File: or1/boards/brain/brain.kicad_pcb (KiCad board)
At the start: 4 copper layers, 78 x 39 mm, 99 parts, among them J1 XILINX_JTAG, J2 BARREL_JACK, J3 Conn_01x03, J4 Conn_01x05, J5 CONN_SKY130_TEST_HOST, J6 Conn_01x03, U1 STM32F031-QFN28, U2 XC7S15-1FTGB196C, U3 ADP323, U4 S25FL128SAGBHI300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

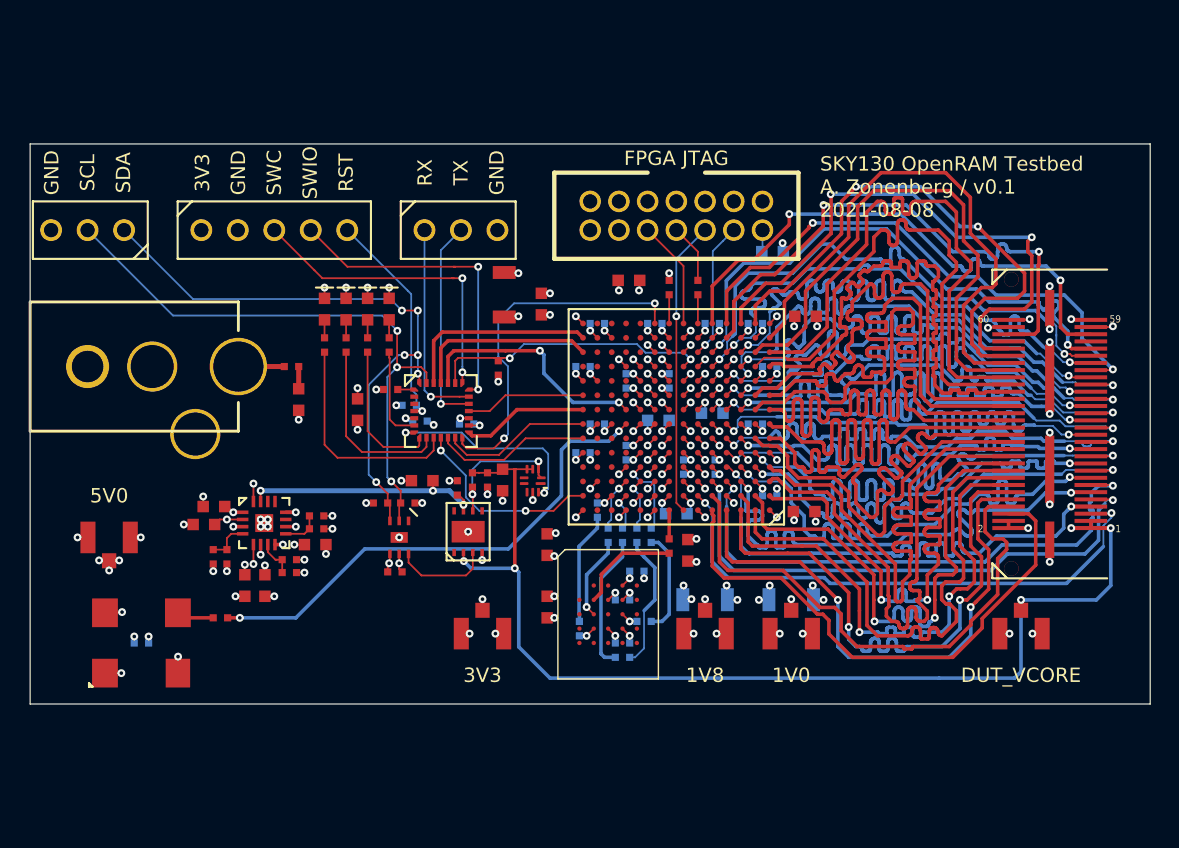
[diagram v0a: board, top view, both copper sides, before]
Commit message: Updated brain board with silkscreen logos and mounting holes
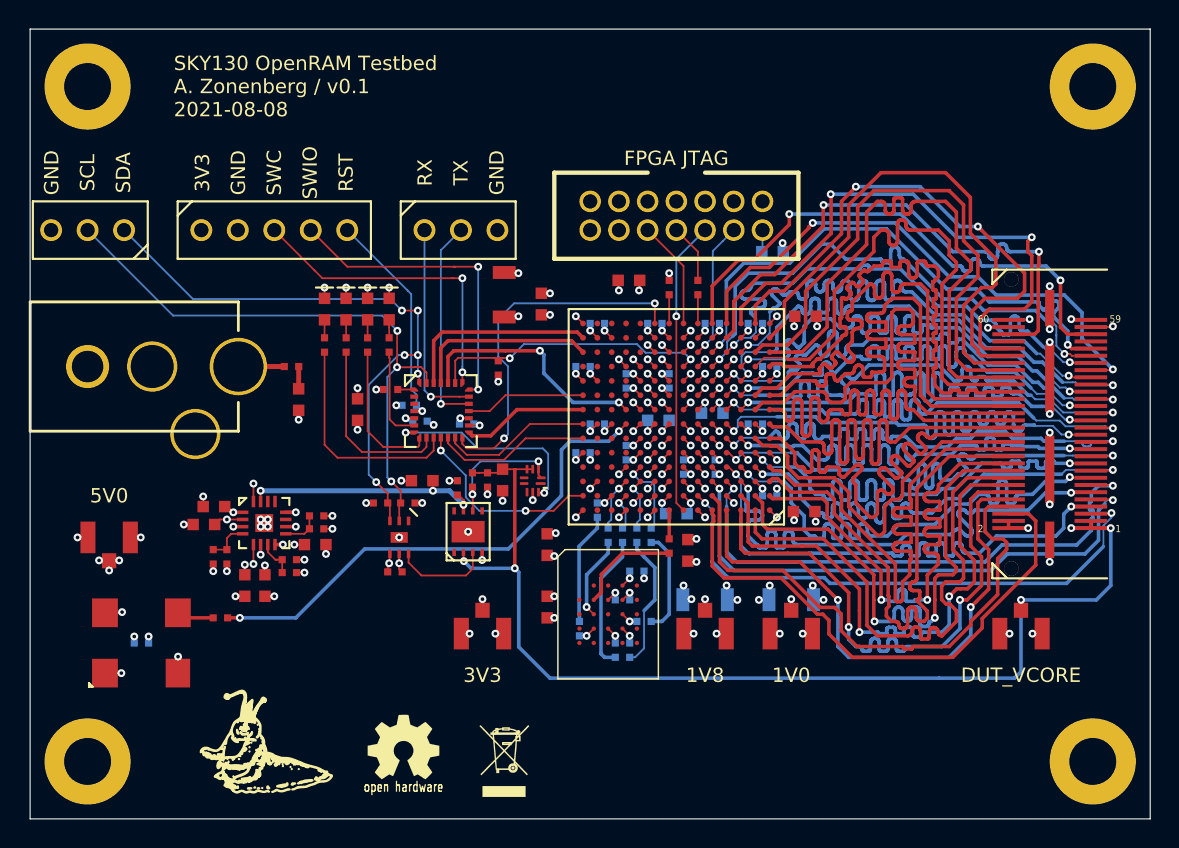
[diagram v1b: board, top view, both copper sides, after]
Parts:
- added G***: LOGO, w_logo:Logo_silk_WEEE_3.4x5mm, F.Cu at (73.0, 87.0)
- added G***: LOGO, w_logo:Logo_silk_OSHW_6x6mm, F.Cu at (66.0, 86.0)
- added G***: LOGO, azonenberg_pcb:LONGTHING-1200DPI, F.Cu at (57.0, 86.0)
- added MH1: SCREWHOLE_4_40, azonenberg_pcb:MECHANICAL_CLEARANCEHOLE_4_40, F.Cu at (44.0, 40.0)
- added MH2: SCREWHOLE_4_40, azonenberg_pcb:MECHANICAL_CLEARANCEHOLE_4_40, F.Cu at (44.0, 87.0)
- added MH3: SCREWHOLE_4_40, azonenberg_pcb:MECHANICAL_CLEARANCEHOLE_4_40, F.Cu at (114.0, 40.0)
- added MH4: SCREWHOLE_4_40, azonenberg_pcb:MECHANICAL_CLEARANCEHOLE_4_40, F.Cu at (114.0, 87.0)
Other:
- board size 78 x 39 mm -> 78 x 55 mm

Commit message: Finished initial routing. Ready for layout review.
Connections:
- J5 pad 10: /DUT socket/ADDR0_5 -> /DUT socket/DIN0_7
- J5 pad 11: /DUT socket/ADDR0_6 -> /DUT socket/ADDR1_1
- J5 pad 12: /DUT socket/ADDR0_7 -> /DUT socket/ADDR1_6
- J5 pad 14: /DUT socket/ADDR1_1 -> /DUT socket/DOUT0_6
- J5 pad 15: /DUT socket/ADDR1_2 -> /DUT socket/DOUT1_0
- J5 pad 16: /DUT socket/ADDR1_3 -> /DUT socket/ADDR1_7
- J5 pad 17: /DUT socket/ADDR1_4 -> /DUT socket/DOUT1_3
- J5 pad 18: /DUT socket/ADDR1_5 -> /DUT socket/DIN0_6
- J5 pad 19: /DUT socket/ADDR1_6 -> /DUT socket/DOUT1_4
- J5 pad 20: /DUT socket/ADDR1_7 -> /DUT socket/DOUT0_5
- J5 pad 21: /DUT socket/DOUT0_0 -> /DUT socket/DOUT1_5
- J5 pad 22: /DUT socket/DOUT0_1 -> /DUT socket/DIN0_5
- J5 pad 23: /DUT socket/DOUT0_2 -> /DUT socket/DOUT1_6
- J5 pad 24: /DUT socket/DOUT0_3 -> /DUT socket/DOUT0_4
- J5 pad 25: /DUT socket/DOUT0_4 -> /DUT socket/DOUT1_7
- J5 pad 26: /DUT socket/DOUT0_5 -> /DUT socket/DIN0_4
- J5 pad 27: /DUT socket/DOUT0_6 -> /DUT socket/DOUT1_1
- J5 pad 28: /DUT socket/DOUT0_7 -> /DUT socket/DOUT0_3
- J5 pad 29: /DUT socket/DIN0_0 -> /DUT socket/DOUT1_2
- J5 pad 30: /DUT socket/DIN0_1 -> /DUT socket/DIN0_3
- J5 pad 31: /DUT socket/DIN0_2 -> /DUT socket/ADDR0_7
- J5 pad 32: /DUT socket/DIN0_3 -> /DUT socket/DIN0_2
- J5 pad 33: /DUT socket/DIN0_4 -> /DUT socket/ADDR0_6
- J5 pad 34: /DUT socket/DIN0_5 -> /DUT socket/DOUT0_2
- J5 pad 35: /DUT socket/DIN0_6 -> /DUT socket/ADDR0_5
- J5 pad 36: /DUT socket/DIN0_7 -> /DUT socket/DOUT0_0
- J5 pad 37: /DUT socket/DOUT1_0 -> /DUT socket/ADDR0_4
- J5 pad 38: /DUT socket/DOUT1_1 -> /DUT socket/DIN0_1
- J5 pad 39: /DUT socket/DOUT1_2 -> /DUT socket/ADDR0_3
- J5 pad 40: /DUT socket/DOUT1_3 -> /DUT socket/DIN0_0
- J5 pad 41: /DUT socket/DOUT1_4 -> /DUT socket/ADDR0_2
- J5 pad 42: /DUT socket/DOUT1_5 -> /DUT socket/DOUT0_1
- J5 pad 43: /DUT socket/DOUT1_6 -> /DUT socket/ADDR0_1
- J5 pad 44: /DUT socket/DOUT1_7 -> /DUT socket/ADDR0_0
- J5 pad 47: /DUT socket/WMASK0_0 -> /DUT socket/WMASK0_2
- J5 pad 48: /DUT socket/WMASK0_1 -> /DUT socket/WMASK0_3
- J5 pad 49: /DUT socket/WMASK0_2 -> /DUT socket/WMASK0_1
- J5 pad 5: /DUT socket/ADDR0_0 -> /DUT socket/ADDR1_4
- J5 pad 50: /DUT socket/WMASK0_3 -> /DUT socket/WE0_N
- J5 pad 51: /DUT socket/WE0_N -> /DUT socket/WMASK0_0
- J5 pad 6: /DUT socket/ADDR0_1 -> /DUT socket/DOUT0_7
- J5 pad 7: /DUT socket/ADDR0_2 -> /DUT socket/ADDR1_3
- J5 pad 8: /DUT socket/ADDR0_3 -> /DUT socket/ADDR1_5
- J5 pad 9: /DUT socket/ADDR0_4 -> /DUT socket/ADDR1_2
- U2 pad A2: /DUT socket/ADDR1_3 -> /DUT socket/ADDR1_7
- U2 pad A3: /DUT socket/ADDR0_7 -> /DUT socket/ADDR1_6
- U2 pad A4: /DUT socket/ADDR0_5 -> /DUT socket/DIN0_7
- U2 pad A5: /DUT socket/ADDR0_1 -> /DUT socket/DOUT0_7
- U2 pad B1: /DUT socket/ADDR1_7 -> /DUT socket/DOUT0_5
- U2 pad B2: /DUT socket/ADDR1_5 -> /DUT socket/DIN0_6
- U2 pad B3: /DUT socket/ADDR1_1 -> /DUT socket/DOUT0_6
- U2 pad B5: /DUT socket/ADDR0_3 -> /DUT socket/ADDR1_5
- U2 pad B6: /DUT socket/ADDR0_0 -> /DUT socket/ADDR1_4
- U2 pad C1: /DUT socket/DOUT0_1 -> /DUT socket/DIN0_5
- U2 pad C3: /DUT socket/ADDR0_6 -> /DUT socket/ADDR1_1
- U2 pad C5: /DUT socket/ADDR0_4 -> /DUT socket/ADDR1_2
- U2 pad D1: /DUT socket/DOUT0_3 -> /DUT socket/DOUT0_4
- U2 pad D2: /DUT socket/ADDR1_4 -> /DUT socket/DOUT1_3
- U2 pad D3: /DUT socket/ADDR1_2 -> /DUT socket/DOUT1_0
- U2 pad D4: /DUT socket/ADDR0_2 -> /DUT socket/ADDR1_3
- U2 pad E2: /DUT socket/ADDR1_6 -> /DUT socket/DOUT1_4
- U2 pad E4: /DUT socket/DOUT0_0 -> /DUT socket/DOUT1_5
- U2 pad F1: /DUT socket/DOUT0_7 -> /DUT socket/DOUT0_3
- U2 pad F2: /DUT socket/DOUT0_5 -> /DUT socket/DIN0_4
- U2 pad F3: /DUT socket/DOUT0_2 -> /DUT socket/DOUT1_6
- U2 pad F4: /DUT socket/DOUT0_4 -> /DUT socket/DOUT1_7
- U2 pad G1: /DUT socket/DIN0_1 -> /DUT socket/DIN0_3
- U2 pad G4: /DUT socket/DOUT0_6 -> /DUT socket/DOUT1_1
- U2 pad H1: /DUT socket/DIN0_3 -> /DUT socket/DIN0_2
- U2 pad H2: /DUT socket/DIN0_5 -> /DUT socket/DOUT0_2
- U2 pad H3: /DUT socket/DIN0_2 -> /DUT socket/ADDR0_7
- U2 pad H4: /DUT socket/DIN0_0 -> /DUT socket/DOUT1_2
- U2 pad J1: /DUT socket/DIN0_7 -> /DUT socket/DOUT0_0
- U2 pad J2: /DUT socket/DOUT1_1 -> /DUT socket/DIN0_1
- U2 pad J3: /DUT socket/DIN0_6 -> /DUT socket/ADDR0_5
- U2 pad J4: /DUT socket/DIN0_4 -> /DUT socket/ADDR0_6
- U2 pad K3: /DUT socket/DOUT1_4 -> /DUT socket/ADDR0_2
- U2 pad K4: /DUT socket/DOUT1_0 -> /DUT socket/ADDR0_4
- U2 pad L1: /DUT socket/DOUT1_3 -> /DUT socket/DIN0_0
- U2 pad L2: /DUT socket/DOUT1_5 -> /DUT socket/DOUT0_1
- U2 pad L3: /DUT socket/DOUT1_2 -> /DUT socket/ADDR0_3
- U2 pad L5: /DUT socket/WMASK0_2 -> /DUT socket/WMASK0_1
- U2 pad M1: /DUT socket/DOUT1_7 -> /DUT socket/ADDR0_0
- U2 pad M3: /DUT socket/DOUT1_6 -> /DUT socket/ADDR0_1
- U2 pad M4: /DUT socket/WMASK0_0 -> /DUT socket/WMASK0_2
- U2 pad M5: /DUT socket/WE0_N -> /DUT socket/WMASK0_0
- U2 pad N1: /DUT socket/WMASK0_1 -> /DUT socket/WMASK0_3
- U2 pad P2: /DUT socket/WMASK0_3 -> /DUT socket/WE0_N
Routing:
- net /DUT socket/DIN0_2: track 42.2 -> 16.9 mm, vias 2 -> 0
- net /DUT socket/DOUT0_3: track 38.0 -> 16.7 mm
- net /DUT socket/DIN0_3: track 38.0 -> 16.7 mm
- net /DUT socket/DOUT0_4: track 38.1 -> 17.3 mm, vias 2 -> 0
- net /DUT socket/DOUT0_0: track 37.9 -> 17.8 mm, vias 2 -> 0
- net /DUT socket/DIN0_4: track 38.1 -> 17.9 mm, vias 2 -> 0
- net /DUT socket/DIN0_5: track 38.1 -> 18.1 mm
- net /DUT socket/DOUT0_2: track 38.0 -> 18.2 mm, vias 2 -> 0
- net /DUT socket/DIN0_1: track 38.0 -> 19.0 mm
- net /DUT socket/DIN0_6: track 38.0 -> 20.7 mm, vias 2 -> 0
- net /DUT socket/DOUT0_1: track 37.9 -> 20.9 mm
- net /DUT socket/DIN0_0: track 38.0 -> 22.3 mm, vias 2 -> 0
- net /DUT socket/ADDR1_7: track 38.1 -> 22.5 mm, vias 2 -> 0
- net /DUT socket/DOUT0_6: track 38.1 -> 25.1 mm, vias 2 -> 0
- net /DUT socket/ADDR1_6: track 37.9 -> 25.2 mm, vias 2 -> 0
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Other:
- board text added: "SKY130 OpenRAM Testbed A. Zonenberg / v0.1 2021-11-05"
- board text removed: "SKY130 OpenRAM Testbed A. Zonenberg / v0.1 2021-08-08"

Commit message: Final rev of brain after layout review
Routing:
- net /DUT socket/CS0_N: track 38.1 -> 28.0 mm
- net /DUT socket/GPIO0: track 40.2 -> 31.3 mm, vias 2 -> 0
- net /DUT socket/WMASK0_3: track 38.0 -> 30.1 mm
- net /DUT socket/ADDR0_6: track 38.1 -> 45.0 mm
- net /DUT socket/ADDR0_5: track 38.0 -> 43.1 mm
- net /DUT socket/ADDR0_4: track 38.0 -> 42.9 mm
- net /DUT socket/ADDR0_3: track 38.0 -> 42.1 mm
- net /DUT socket/ADDR0_2: track 38.0 -> 42.0 mm
- net /DUT socket/ADDR1_0: track 38.1 -> 42.0 mm
- net /DUT socket/WE0_N: track 38.0 -> 35.1 mm, vias 2 -> 0
- net /DUT socket/CS1_N: track 36.7 -> 34.6 mm, vias 2 -> 0
- net /DUT socket/CLK0: track 38.0 -> 40.0 mm
- net /DUT socket/CLK1: track 38.0 -> 36.8 mm
- net /DUT socket/ADDR0_0: track 25.9 -> 27.0 mm
- net /DUT socket/ADDR0_1: track 42.1 -> 41.0 mm
- added copper zone on B.Cu, net /DUT_VCORE
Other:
- board text added: "SKY130 OpenRAM Testbed A. Zonenberg / v0.1 2021-11-06"
- board text removed: "SKY130 OpenRAM Testbed A. Zonenberg / v0.1 2021-11-05"
